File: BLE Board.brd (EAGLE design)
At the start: 51.3 x 67 mm, 39 parts, among them IC1 TM4C123GH6PM, IC2 TPS6300

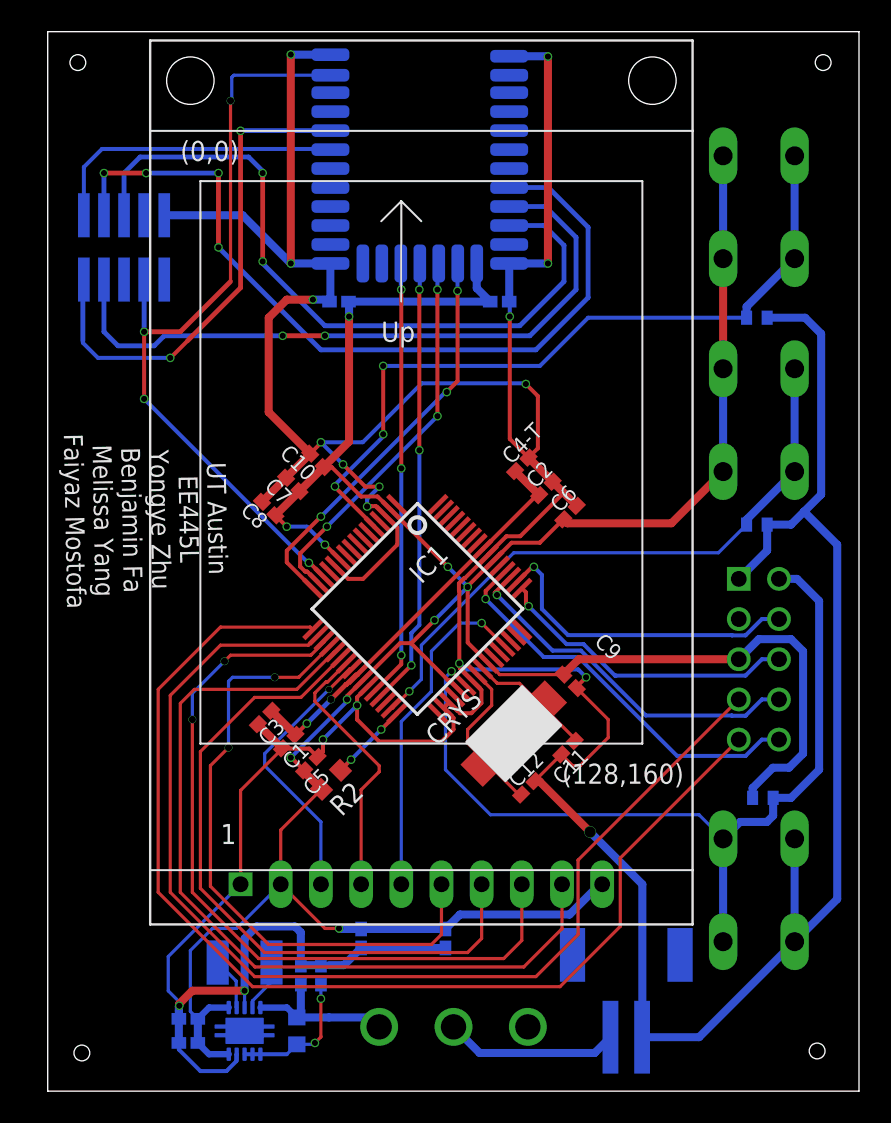
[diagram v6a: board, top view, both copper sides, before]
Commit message: Moved power reg., changed some parts
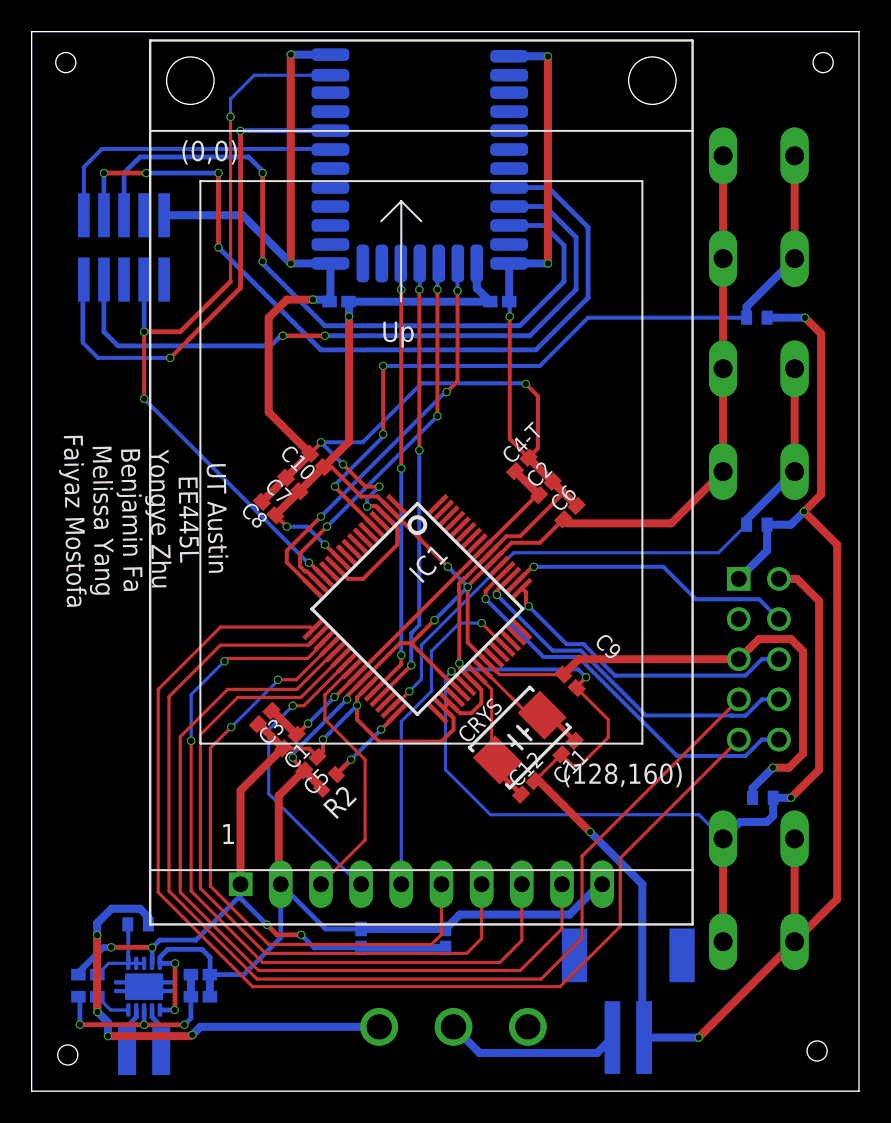
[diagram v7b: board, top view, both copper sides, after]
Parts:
- removed L1: 2.2uH, inductor-neosid:MS50
- added I1: (no value), 445L_final:IND_LPS3015
- CRYS: device EE445L:NX5032GA -> NX5032GA:2-SMD-5X3
- R2, R3: device EE445L:R0603 -> EE445L:R0402
- moved C15 14.7 mm to (-3.05, 7.37), turned to 0 degrees
- moved C16 13.5 mm to (-3.05, 5.97), turned to 0 degrees
- moved R3 12.1 mm to (0.13, 10.5), turned to 180 degrees
- moved IC2 6.94 mm to (0.51, 6.60), turned to 0 degrees
- moved C13 4.38 mm to (4.06, 7.37)
- moved C14 1.59 mm to (4.06, 5.97)
- moved CRYS 0.46 mm to (24.3, 22.4)
- moved R2 0.18 mm to (12.2, 19.6)
- moved B1 0.13 mm to (31.1, 7.09)
- moved C1 0.08 mm to (9.73, 22.1)
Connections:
- new net PGND: C13.2, C14.2, C16.2, IC2.3
- net GND: no longer C13.2, C14.2, C16.2, IC2.3
- net N$3: now also I1.2; no longer L1.1
- net N$4: now also I1.1; no longer L1.2
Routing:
- net IN: track 10.2 -> 32.4 mm, vias 0 -> 4
- net GND: track 320.7 -> 307.5 mm, vias 18 -> 23
- net PGND: track 0.00 -> 12.7 mm, vias 0 -> 3
- net N$1: track 8.62 -> 5.73 mm, vias 2 -> 0
- net +3V3: track 193.7 -> 196.6 mm, vias 9 -> 11
- net TDI: track 20.5 -> 18.4 mm
- net C/D: track 17.0 -> 18.9 mm, vias 0 -> 1
- net TFT_CS: track 40.3 -> 38.5 mm
- net OSC1: track 10.1 -> 8.74 mm
- net MISO: track 53.0 -> 51.9 mm
- net RESET: track 17.5 -> 16.6 mm, vias 1 -> 0
- net BGM_RST: track 49.6 -> 48.8 mm
- net MOSI: track 43.2 -> 43.9 mm
- net N$3: track 3.34 -> 2.83 mm
- net N$4: track 3.34 -> 2.83 mm
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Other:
- board size 51.3 x 67 mm -> 52.3 x 67 mm
